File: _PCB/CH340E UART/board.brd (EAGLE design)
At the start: 24.9 x 16.3 mm, 11 parts, among them IC1 REG1117, U1 CH340ESMD

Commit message: CH340e design complete
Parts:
- removed D1: 1206size, SparkFun-LED:LED-1206
- removed J1: (no value), SparkFun-Connectors:USB-MICROB
- removed U1: CH340ESMD, CH340E:MSOP10
- added CH340E: CH340ESMD, CH340E:MSOP10
- added LED1: (no value), adafruit:CHIPLED_0805
- added USB2: ST-USB-001G, Seeed-Connector:MICRO-USB5+4P-SMD-0.65-B
- JP1: device SparkFun-Jumpers:SMT-JUMPER_3_1-NC_PASTE_SILK -> SparkFun-Jumpers:SMT-JUMPER_3_NO_SILK
- moved C4 19.1 mm to (2.54, 2.03), turned to 180 degrees
- moved C5 13.2 mm to (15.0, 2.03)
- moved C6 5.59 mm to (15.0, 14.5), turned to 180 degrees
- moved J2 3.30 mm to (19.6, 1.78)
- moved JP1 2.65 mm to (8.89, 14.5)
- moved IC1 2.54 mm to (9.40, 5.59), turned to 180 degrees
- moved J3 2.54 mm to (12.2, 11.9)
- moved C3 0.25 mm to (2.54, 14.5), turned to 180 degrees
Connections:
- net 5V1 renamed 3V3
- net 5V: now also USB2.1; no longer J1.VBUS
- net CTS: now also CH340E.5; no longer U1.5
- net GND: now also CH340E.3, LED1.C, USB2.5, USB2.S1, USB2.S2, USB2.S3, USB2.S4, USB2.S5, USB2.S6; no longer D1.C, J1.GND, U1.3
- net N$1: now also CH340E.6, LED1.A; no longer D1.A, U1.6
- net RTS: now also CH340E.4; no longer U1.4
- net RX: now also CH340E.9; no longer U1.9
- net TX: now also CH340E.8; no longer U1.8
- net USBN: now also CH340E.2, USB2.2; no longer J1.D-, U1.2
- net USBP: now also CH340E.1, USB2.3; no longer J1.D+, U1.1
- net VCC: now also CH340E.10, CH340E.7; no longer U1.10, U1.7
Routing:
- net GND: track 64.6 -> 1.06 mm, vias 2 -> 0
- net VCC: track 40.4 -> 24.0 mm, vias 0 -> 3
- net 5V: track 31.0 -> 24.4 mm, vias 2 -> 3
- net TX: track 17.3 -> 11.1 mm, vias 0 -> 1
- net CTS: track 10.1 -> 4.71 mm, vias 1 -> 0
- net RX: track 11.1 -> 6.59 mm
- net N$1: track 7.79 -> 4.32 mm
- net RTS: track 8.66 -> 5.47 mm
- net 3V3: track 13.8 -> 16.9 mm
- net USBN: track 14.8 -> 15.5 mm
- net USBP: track 11.2 -> 11.3 mm, vias 0 -> 2
- added copper zone on layer 1, net GND
- added copper zone on layer 16, net GND
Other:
- board size 24.9 x 16.3 mm -> 21.1 x 15.2 mm
- board text added: "CTS"
- board text added: "GND"
- board text added: "RTS"
- board text added: "RX"
- board text added: "TX"
- board text added: "VCC"

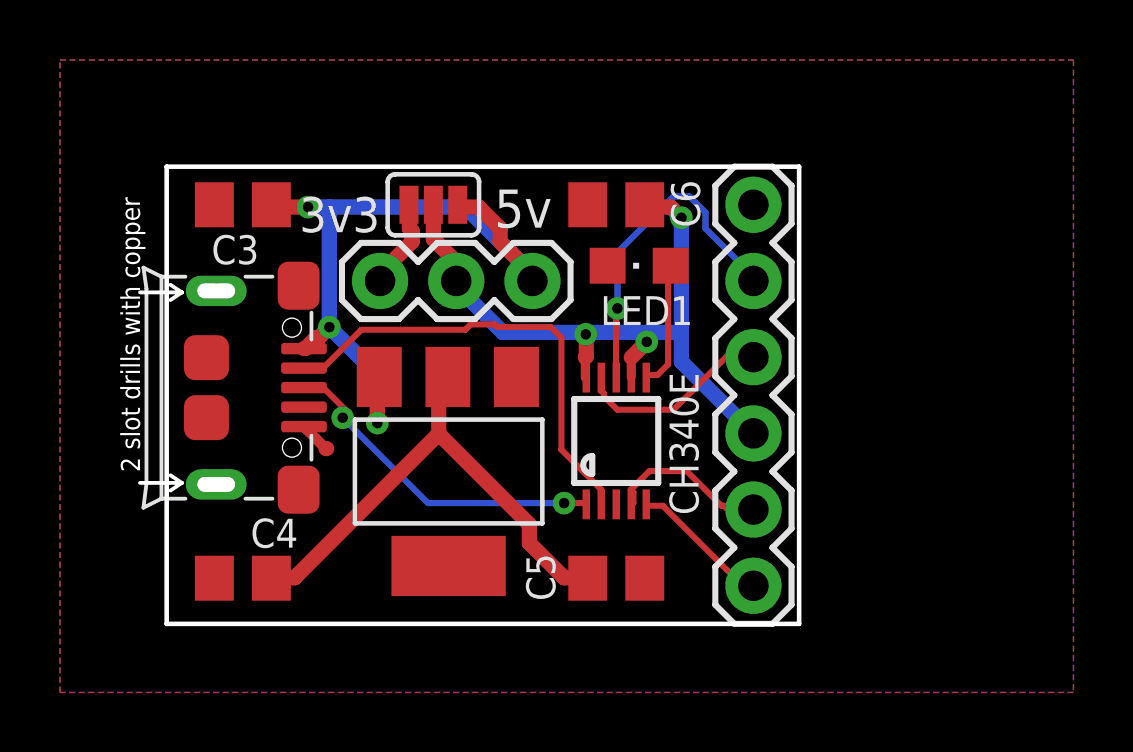
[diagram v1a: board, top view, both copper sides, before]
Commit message: CH340E converter complete + LoRa sensor node
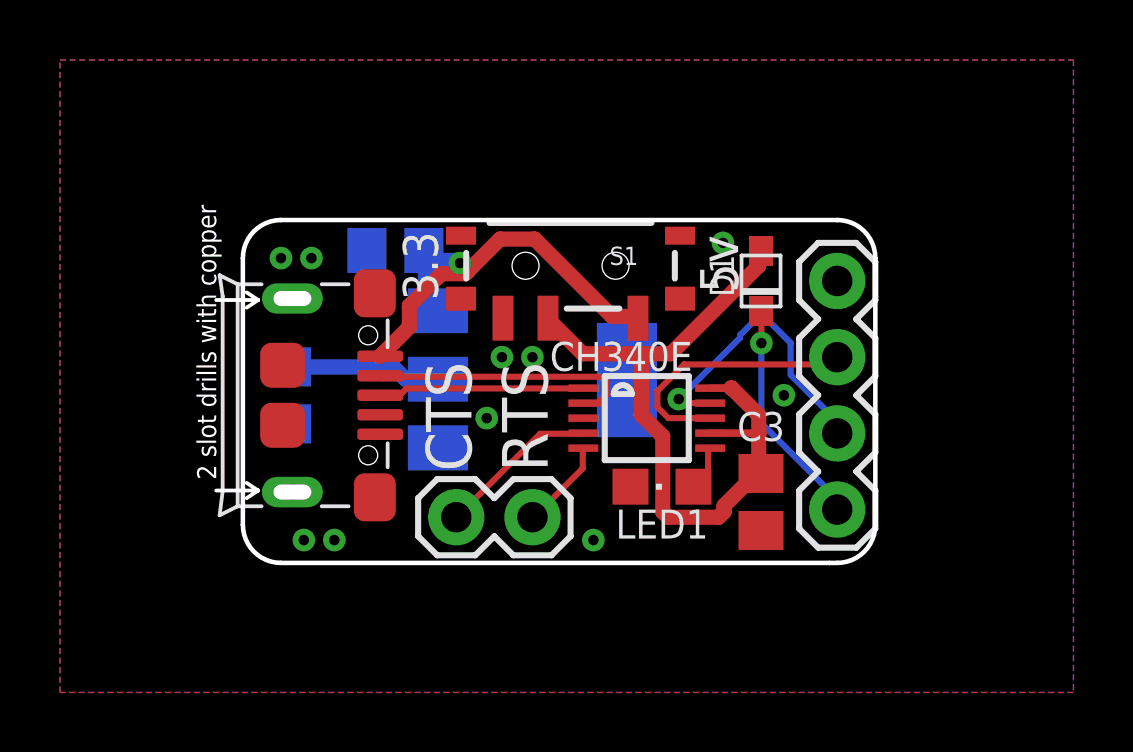
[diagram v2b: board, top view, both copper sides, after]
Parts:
- removed C4, C5, C6: 100nF, rcl-2:C0805
- removed J3: (no value), SparkFun-Connectors:1X03
- removed JP1: (no value), SparkFun-Jumpers:SMT-JUMPER_3_NO_SILK
- added C1, C2: 100nF, rcl-2:C0805
- added D1: (no value), adafruit:SOD-323F
- added J1: (no value), SparkFun-Connectors:1X04
- added S1: (no value), SparkFun-Switches:SWITCH_SPST_SMD_A
- J2: device SparkFun-Connectors:1X06 -> SparkFun-Connectors:1X02
- moved C3 19.9 mm to (19.8, 4.57), turned to 270 degrees
- moved J2 7.71 mm to (12.2, 4.06), turned to 180 degrees
- moved LED1 7.41 mm to (16.5, 5.08)
- moved IC1 4.13 mm to (12.2, 8.64), flipped to the bottom, turned to 90 degrees
- moved USB2 2.55 mm to (7.37, 8.13)
- moved CH340E 1.27 mm to (16.0, 7.37), turned to 0 degrees
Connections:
- new net VCC_D: D1.C, J1.1
- net 3.3V: now also S1.1; no longer J3.3, JP1.1
- net 3V3: now also C2.1; no longer C4.1, C5.1
- net 5V: now also C1.1, S1.3; no longer C3.1, J3.1, JP1.3
- net GND: now also C1.2, C2.2, J1.4; no longer C4.2, C5.2, C6.2, J2.6
- net RX: now also J1.2; no longer J2.4
- net TX: now also J1.3; no longer J2.5
- net VCC: now also C3.1, D1.A, S1.2; no longer C6.1, J2.3, J3.2, JP1.2
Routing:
- net 3V3: track 16.9 -> 5.15 mm
- net 5V: track 24.4 -> 15.7 mm, vias 3 -> 1
- net VCC_D: track 0.00 -> 7.68 mm, vias 0 -> 1
- net USBN: track 15.5 -> 9.02 mm
- net USBP: track 11.3 -> 6.86 mm, vias 2 -> 0
- net RX: track 6.59 -> 9.90 mm, vias 0 -> 1
- net 3.3V: track 3.02 -> 0.00 mm
- net N$1: track 4.32 -> 1.55 mm
- net TX: track 11.1 -> 8.92 mm, vias 1 -> 0
- net CTS: track 4.71 -> 3.02 mm
- net GND: track 1.06 -> 0.00 mm, vias 0 -> 10
- net VCC: track 24.0 -> 24.5 mm, vias 3 -> 0
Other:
- board size 21.1 x 15.2 mm -> 21.1 x 11.4 mm
- board text added: "3.3"
- board text removed: "3v3"
